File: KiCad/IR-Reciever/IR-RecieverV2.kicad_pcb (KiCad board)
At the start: 2 copper layers, 19.7 x 17.8 mm, 6 parts, among them P1 CONN_6, U1 TSOP38238, U2 TSOP38238, U3 TSOP38238, U4 RGBLED

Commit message: Through Holes & Player/Health Schematic
I'm re-uploading the Apparel Sensor and Weapon PCBs with extended edges
and through holes on the corners for mounting. This also includes the
first draft of the Player/Health Schematic. Please critique
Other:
- board size 19.7 x 17.8 mm -> 19.7 x 25.3 mm
- board text added: "Apparel Sensor Array PCB v1"
- board text added: "LaZIR Tag April 2015"
- board text removed: "Apparel Sensor Array v1"
- board text removed: "LaZIR Tag March 2015"
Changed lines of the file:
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@@
     (links 15)
     (no_connects 0)
-    (area 24.7904 20.7518 48.3362 41.7322)
+    (area 24.7904 18.428499 48.3362 43.801501)
     (thickness 1.6)
-    (drawings 6)
+    (drawings 17)
     (tracks 21)
     (zones 0)
@@
     )
   )
-  (gr_text "Apparel Sensor Array v1" (at 45.974 22.86) (layer F.SilkS)
+  (gr_circle (center 44.1325 41.8465) (end 45.847 41.8465) (layer Edge.Cuts) (width 0.1))
+  (gr_circle (center 28.8925 41.8465) (end 30.607 41.8465) (layer Edge.Cuts) (width 0.1))
+  (gr_circle (center 44.1325 20.3835) (end 44.1325 18.669) (layer Edge.Cuts) (width 0.1))
+  (gr_circle (center 28.8925 20.3835) (end 27.178 20.3835) (layer Edge.Cuts) (width 0.1))
+  (gr_line (start 26.67 22.0345) (end 26.67 20.32) (angle 90) (layer Edge.Cuts) (width 0.1))
+  (gr_line (start 26.67 22.225) (end 26.67 22.0345) (angle 90) (layer Edge.Cuts) (width 0.1))
+  (gr_line (start 26.67 18.4785) (end 26.67 18.669) (angle 90) (layer Edge.Cuts) (width 0.1))
+  (gr_line (start 46.355 18.4785) (end 46.355 22.225) (angle 90) (layer Edge.Cuts) (width 0.1))
+  (gr_line (start 26.67 18.4785) (end 46.355 18.4785) (angle 90) (layer Edge.Cuts) (width 0.1))
+  (gr_line (start 26.67 22.225) (end 26.67 18.4785) (angle 90) (layer Edge.Cuts) (width 0.1))
+  (gr_line (start 46.355 43.7515) (end 46.355 40.005) (angle 90) (layer Edge.Cuts) (width 0.1))
+  (gr_line (start 26.67 43.7515) (end 46.355 43.7515) (angle 90) (layer Edge.Cuts) (width 0.1))
+  (gr_line (start 26.67 40.005) (end 26.67 43.7515) (angle 90) (layer Edge.Cuts) (width 0.1))
+  (gr_text "Apparel Sensor Array PCB v1" (at 45.974 22.86) (layer F.SilkS)
     (effects (font (size 0.5 0.5) (thickness 0.125)) (justify right))
   )
-  (gr_text "LaZIR Tag\nMarch 2015" (at 45.974 38.608) (layer F.SilkS)
+  (gr_text "LaZIR Tag\nApril 2015" (at 45.974 38.608) (layer F.SilkS)
     (effects (font (size 0.5 0.5) (thickness 0.125)) (justify right))
   )
   (gr_line (start 26.67 40.005) (end 26.67 22.225) (angle 90) (layer Edge.Cuts) (width 0.1))
-  (gr_line (start 46.355 40.005) (end 26.67 40.005) (angle 90) (layer Edge.Cuts) (width 0.1))
   (gr_line (start 46.355 22.225) (end 46.355 40.005) (angle 90) (layer Edge.Cuts) (width 0.1))
-  (gr_line (start 26.67 22.225) (end 46.355 22.225) (angle 90) (layer Edge.Cuts) (width 0.1))
   (segment (start 38.1 34.29) (end 38.1 37.465) (width 0.254) (layer F.Cu) (net 1))
   (segment (start 39.37 33.02) (end 38.1 34.29) (width 0.254) (layer F.Cu) (net 1))

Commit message: Quick Update #1 4/16
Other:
- board size 19.7 x 25.3 mm -> 19.7 x 27.8 mm
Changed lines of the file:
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@@
     (area 24.7904 18.428499 48.3362 43.801501)
     (thickness 1.6)
-    (drawings 17)
+    (drawings 22)
     (tracks 21)
     (zones 0)
@@
     )
   )
-  (gr_circle (center 44.1325 41.8465) (end 45.847 41.8465) (layer Edge.Cuts) (width 0.1))
-  (gr_circle (center 28.8925 41.8465) (end 30.607 41.8465) (layer Edge.Cuts) (width 0.1))
-  (gr_circle (center 44.1325 20.3835) (end 44.1325 18.669) (layer Edge.Cuts) (width 0.1))
-  (gr_circle (center 28.8925 20.3835) (end 27.178 20.3835) (layer Edge.Cuts) (width 0.1))
+  (gr_circle (center 43.434 20.193) (end 41.7322 20.1676) (layer Edge.Cuts) (width 0.1))
+  (gr_line (start 46.355 17.2085) (end 46.355 18.4785) (angle 90) (layer Edge.Cuts) (width 0.1))
+  (gr_line (start 26.67 17.2085) (end 46.355 17.2085) (angle 90) (layer Edge.Cuts) (width 0.1))
+  (gr_line (start 26.67 22.225) (end 26.67 17.2085) (angle 90) (layer Edge.Cuts) (width 0.1))
+  (gr_line (start 46.355 45.0215) (end 46.355 43.7515) (angle 90) (layer Edge.Cuts) (width 0.1))
+  (gr_line (start 26.67 45.0215) (end 46.355 45.0215) (angle 90) (layer Edge.Cuts) (width 0.1))
+  (gr_line (start 26.67 45.0215) (end 26.67 43.7515) (angle 90) (layer Edge.Cuts) (width 0.1))
+  (gr_circle (center 43.434 42.037) (end 45.1485 42.037) (layer Edge.Cuts) (width 0.1))
+  (gr_circle (center 29.591 42.037) (end 31.3055 42.037) (layer Edge.Cuts) (width 0.1))
+  (gr_circle (center 43.4213 20.1803) (end 43.4213 18.4658) (layer Edge.Cuts) (width 0.1))
+  (gr_circle (center 29.591 20.2057) (end 27.8765 20.2057) (layer Edge.Cuts) (width 0.1))
   (gr_line (start 26.67 22.0345) (end 26.67 20.32) (angle 90) (layer Edge.Cuts) (width 0.1))
   (gr_line (start 26.67 22.225) (end 26.67 22.0345) (angle 90) (layer Edge.Cuts) (width 0.1))
   (gr_line (start 26.67 18.4785) (end 26.67 18.669) (angle 90) (layer Edge.Cuts) (width 0.1))
   (gr_line (start 46.355 18.4785) (end 46.355 22.225) (angle 90) (layer Edge.Cuts) (width 0.1))
-  (gr_line (start 26.67 18.4785) (end 46.355 18.4785) (angle 90) (layer Edge.Cuts) (width 0.1))
   (gr_line (start 26.67 22.225) (end 26.67 18.4785) (angle 90) (layer Edge.Cuts) (width 0.1))
   (gr_line (start 46.355 43.7515) (end 46.355 40.005) (angle 90) (layer Edge.Cuts) (width 0.1))
-  (gr_line (start 26.67 43.7515) (end 46.355 43.7515) (angle 90) (layer Edge.Cuts) (width 0.1))
   (gr_line (start 26.67 40.005) (end 26.67 43.7515) (angle 90) (layer Edge.Cuts) (width 0.1))
-  (gr_text "Apparel Sensor Array PCB v1" (at 45.974 22.86) (layer F.SilkS)
-    (effects (font (size 0.5 0.5) (thickness 0.125)) (justify right))
-  )
-  (gr_text "LaZIR Tag\nApril 2015" (at 45.974 38.608) (layer F.SilkS)
-    (effects (font (size 0.5 0.5) (thickness 0.125)) (justify right))
+  (gr_text "Apparel Sensor\nArray PCB v1" (at 36.4998 18.6944) (layer F.SilkS)
+    (effects (font (size 0.75 0.75) (thickness 0.125)))
+  )
+  (gr_text "LaZIR Tag\nApril 2015" (at 36.195 42.6212) (layer F.SilkS)
+    (effects (font (size 0.75 0.75) (thickness 0.125)))
   )
   (gr_line (start 26.67 40.005) (end 26.67 22.225) (angle 90) (layer Edge.Cuts) (width 0.1))

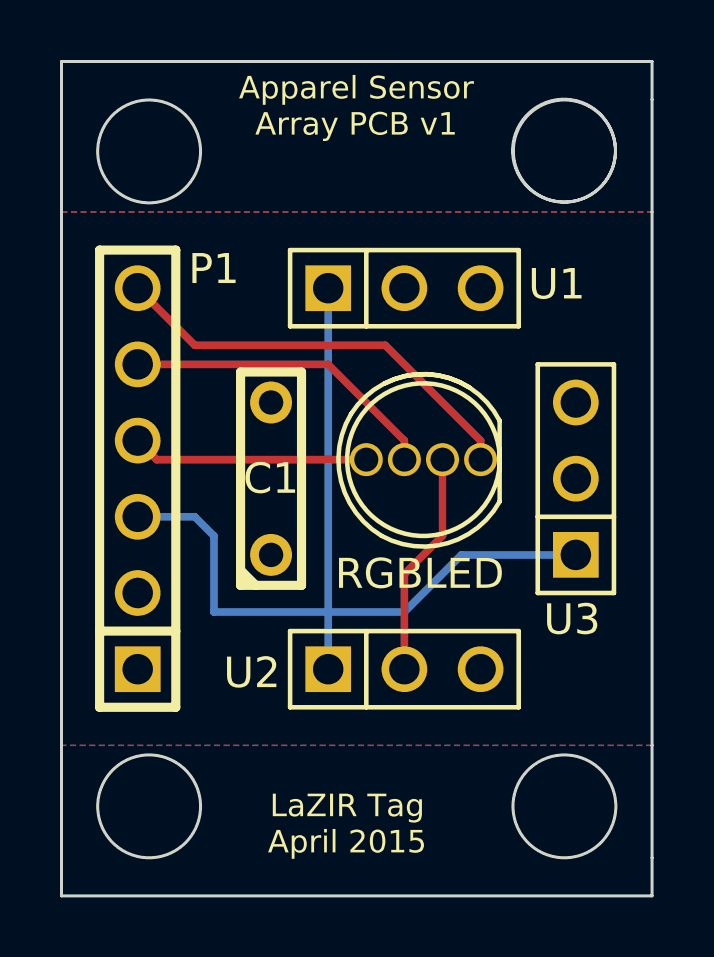
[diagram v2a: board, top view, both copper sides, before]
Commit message: Quick Update #6 4/16
Hopefully the last changes to the ir receiver pcb and weapon pcb
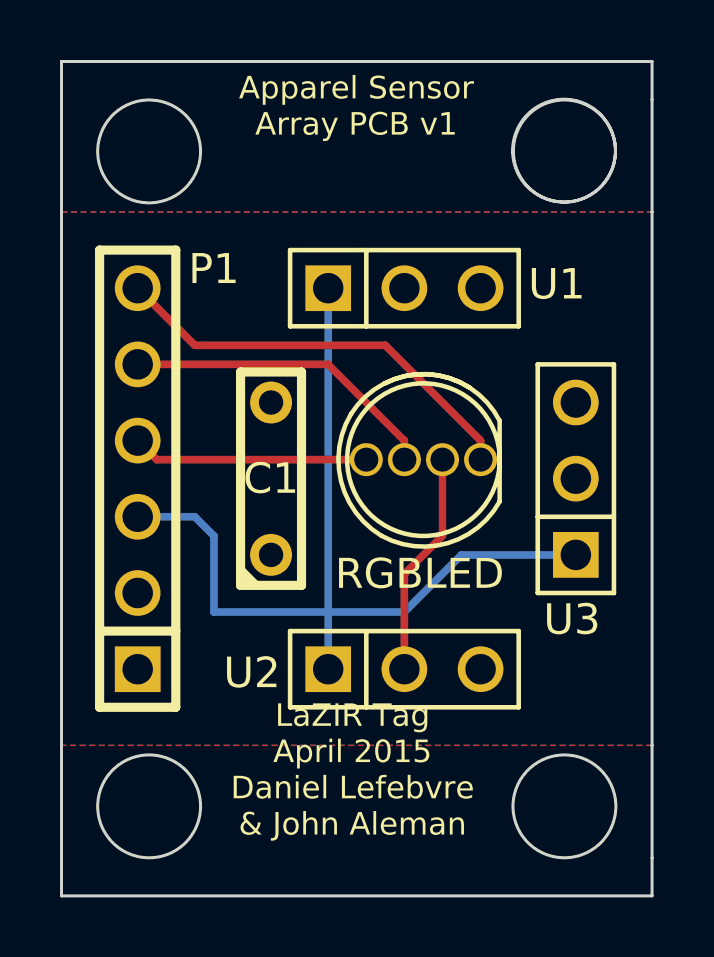
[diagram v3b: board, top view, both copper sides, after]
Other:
- board text added: "LaZIR Tag April 2015 Daniel Lefebvre & John Aleman"
- board text removed: "LaZIR Tag April 2015"
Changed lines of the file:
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@@
     (links 15)
     (no_connects 0)
-    (area 24.7904 18.428499 48.3362 43.801501)
+    (area 24.7904 17.158499 48.3362 45.071501)
     (thickness 1.6)
     (drawings 22)
@@
     (effects (font (size 0.75 0.75) (thickness 0.125)))
   )
-  (gr_text "LaZIR Tag\nApril 2015" (at 36.195 42.6212) (layer F.SilkS)
+  (gr_text "LaZIR Tag\nApril 2015\nDaniel Lefebvre\n& John Aleman" (at 36.3728 40.8178) (layer F.SilkS)
     (effects (font (size 0.75 0.75) (thickness 0.125)))
   )
